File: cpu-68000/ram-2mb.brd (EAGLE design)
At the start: 160 x 100 mm, 54 parts, among them IC101 74HC245DW, IC102 74HC245DW, IC103 74HC245DW, IC104 74HC245DW

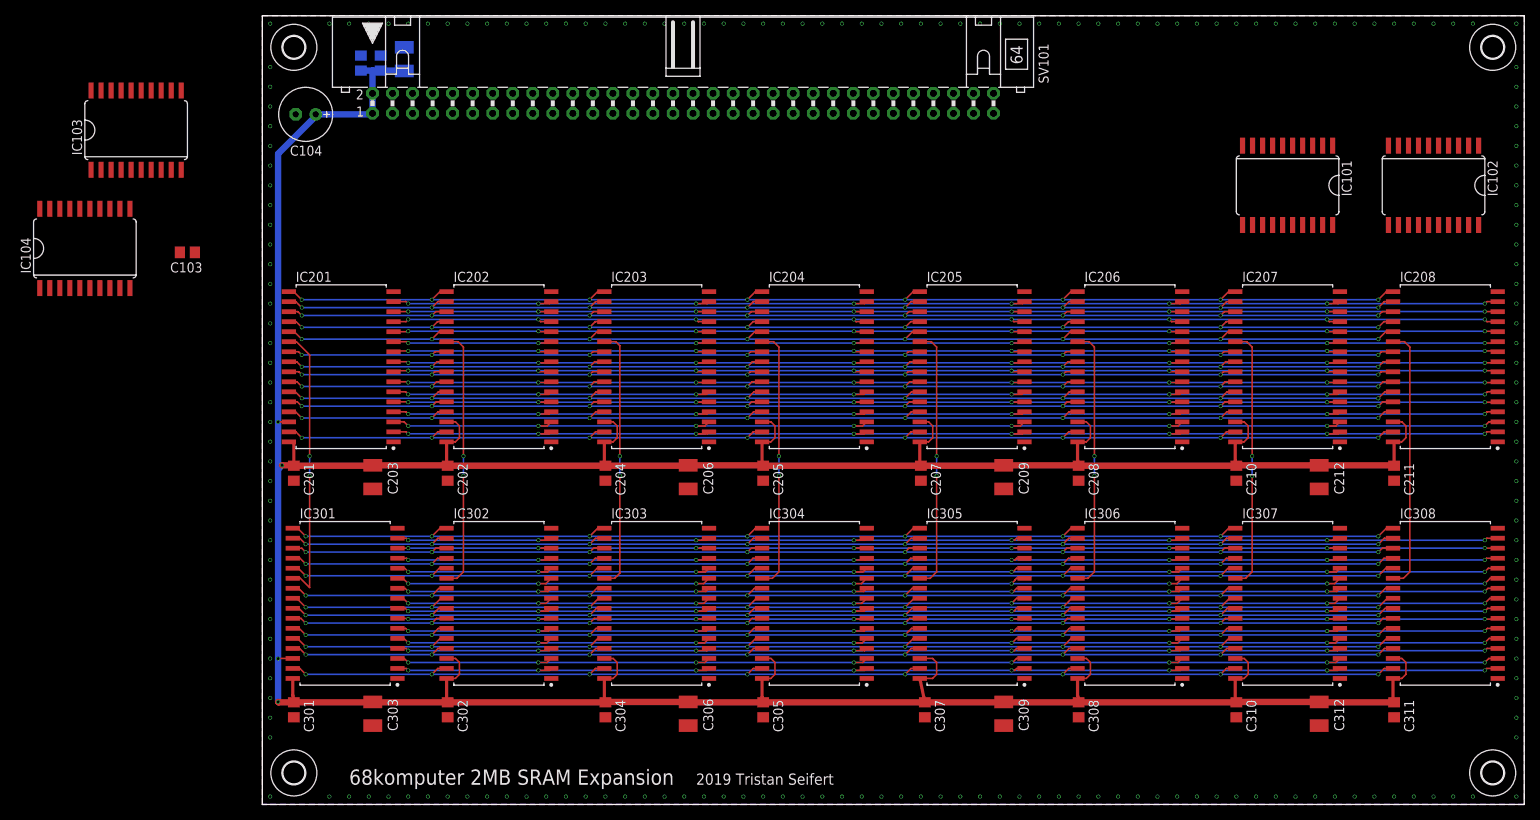
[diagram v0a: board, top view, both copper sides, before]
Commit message: 2MB RAM Expansion: 	- Added decoding logic 	- Started routing bus transceivers 	- Fixed SRAM footprint
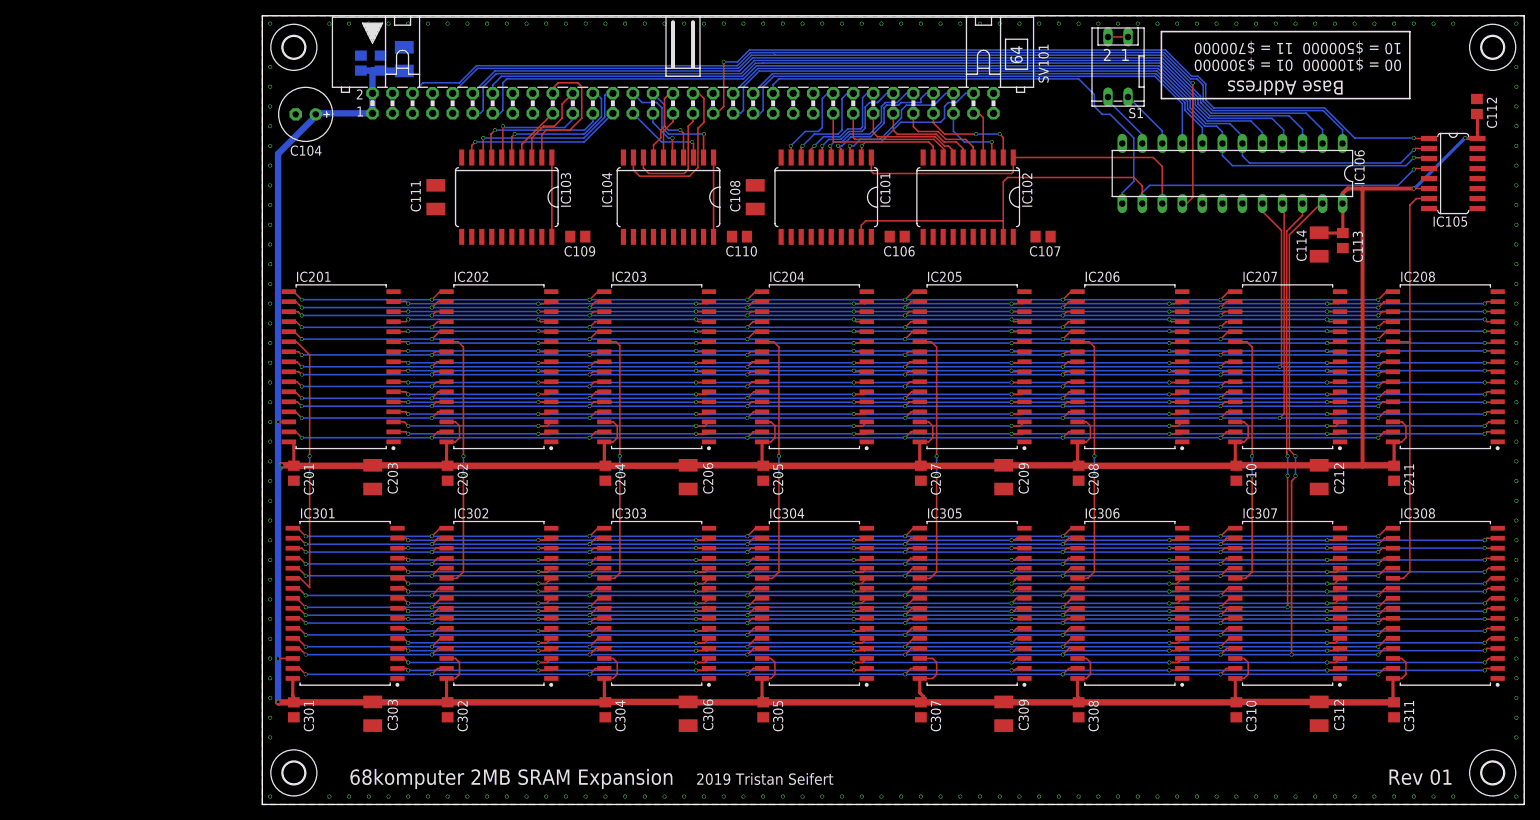
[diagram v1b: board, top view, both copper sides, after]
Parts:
- removed C103: 100nF, rcl:C0805
- added C106, C107, C109, C110, C112, C113: 100nF, rcl:C0805
- added C108, C111, C114: 10µF, rcl:SMC_B
- added IC105: 74HC138D, 74xx-eu:SO16
- added IC106: GAL22V10D, 68komputer:DIL24S
- added S1: (no value), switch-dil:DP-02
- moved IC104 74.3 mm to (51.5, 77.0), turned to 180 degrees
- moved IC102 59.0 mm to (89.5, 77.0)
- moved IC101 58.5 mm to (71.5, 77.0)
- moved IC103 47.8 mm to (31.0, 77.0), turned to 180 degrees
- moved C307 0.50 mm to (83.5, 12.0)
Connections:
- removed net VCC: IC101.20, IC102.20, IC103.20, IC104.20
- new net !CS: IC101.19, IC102.19, IC103.19, IC104.19, IC105.4, IC106.14
- new net !RD: IC101.1, IC102.1, IC106.15
- new net ADDR_SET0: IC106.10, S1.4
- new net ADDR_SET1: IC106.11, S1.3
- new net N$5: IC106.19
- new net N$6: IC106.18
- new net N$7: IC106.17
- net !AS: now also IC106.5
- net !DTACK: now also IC106.16
- net !LDS: now also IC106.3
- net !LOE: now also IC106.20
- net !LWE: now also IC106.21
- net !RAM_CS0: now also IC105.15
- net !RAM_CS1: now also IC105.14
- net !RAM_CS2: now also IC105.13
- net !RAM_CS3: now also IC105.12
- net !RAM_CS4: now also IC105.11
- net !RAM_CS5: now also IC105.10
- net !RAM_CS6: now also IC105.9
- net !RAM_CS7: now also IC105.7
- net !RESET: now also IC106.1
- net !UDS: now also IC106.4
- net !UOE: now also IC106.22
- net !UWE: now also IC106.23
- net +5V: now also C106.1, C107.1, C108.+, C109.1, C110.1, C111.+, C112.1, C113.1, C114.+, IC101.20, IC102.20, IC103.1, IC103.20, IC104.1, IC104.20, IC105.16, IC105.6, IC106.24, S1.1, S1.2; no longer C103.1
- net A1: now also IC103.2
- net A10: now also IC104.3
- net A11: now also IC104.4
- net A12: now also IC104.5
- net A13: now also IC104.6
- net A14: now also IC104.7
- net A15: now also IC104.8
- net A16: now also IC104.9
- net A18: now also IC105.1
- net A19: now also IC105.2, IC106.6
- net A2: now also IC103.3
- net A20: now also IC105.3, IC106.7
- net A21: now also IC106.8
- net A22: now also IC106.9
- net A23: now also IC106.13
- net A3: now also IC103.4
- net A4: now also IC103.5
- net A5: now also IC103.6
- net A6: now also IC103.7
- net A7: now also IC103.8
- net A8: now also IC103.9
- net A9: now also IC104.2
- net D0: now also IC101.2
- net D1: now also IC101.3
- net D10: now also IC102.4
- net D11: now also IC102.5
- net D12: now also IC102.6
- net D13: now also IC102.7
- net D14: now also IC102.8
- net D15: now also IC102.9
- net D2: now also IC101.4
- net D3: now also IC101.5
- net D4: now also IC101.6
- net D5: now also IC101.7
- net D6: now also IC101.8
- net D7: now also IC101.9
- net D8: now also IC102.2
- net D9: now also IC102.3
- net GND: now also C106.2, C107.2, C108.-, C109.2, C110.2, C111.-, C112.2, C113.2, C114.-, IC105.5, IC105.8, IC106.12; no longer C103.2
- net R/!W!: now also IC106.2
- net RAM_A0: now also IC103.18
- net RAM_A1: now also IC103.17
- net RAM_A10: now also IC104.16
- net RAM_A11: now also IC104.15
- net RAM_A12: now also IC104.14
- net RAM_A13: now also IC104.13
- net RAM_A14: now also IC104.12
- net RAM_A15: now also IC104.11
- net RAM_A2: now also IC103.16
- net RAM_A3: now also IC103.15
- net RAM_A4: now also IC103.14
- net RAM_A5: now also IC103.13
- net RAM_A6: now also IC103.12
- net RAM_A7: now also IC103.11
- net RAM_A8: now also IC104.18
- net RAM_A9: now also IC104.17
- net RAM_D0: now also IC101.18
- net RAM_D1: now also IC101.17
- net RAM_D10: now also IC102.16
- net RAM_D11: now also IC102.15
- net RAM_D12: now also IC102.14
- net RAM_D13: now also IC102.13
- net RAM_D14: now also IC102.12
- net RAM_D15: now also IC102.11
- net RAM_D2: now also IC101.16
- net RAM_D3: now also IC101.15
- net RAM_D4: now also IC101.14
- net RAM_D5: now also IC101.13
- net RAM_D6: now also IC101.12
- net RAM_D7: now also IC101.11
- net RAM_D8: now also IC102.18
- net RAM_D9: now also IC102.17
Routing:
- net !RESET: track 0.00 -> 127.0 mm
- net !LDS: track 0.00 -> 115.7 mm
- net R/!W!: track 0.00 -> 115.6 mm
- net !DTACK: track 0.00 -> 113.5 mm, vias 0 -> 1
- net !UDS: track 0.00 -> 108.3 mm
- net !AS: track 0.00 -> 107.6 mm
- net A18: track 0.00 -> 103.2 mm, vias 0 -> 2
- net A20: track 0.00 -> 99.9 mm, vias 0 -> 1
- net A19: track 0.00 -> 97.3 mm, vias 0 -> 1
- net +5V: track 505.1 -> 597.3 mm, vias 4 -> 6
- net !CS: track 0.00 -> 86.2 mm, vias 0 -> 1
- net A22: track 0.00 -> 64.7 mm
- net A21: track 0.00 -> 63.4 mm
- net A23: track 0.00 -> 60.0 mm
- net !UWE: track 153.3 -> 212.9 mm, vias 8 -> 11
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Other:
- board text added: "00 = $100000 01 = $300000 10 = $500000 11 = $700000"
- board text added: "Base Address"
- board text added: "Rev 01"

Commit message: 2MB RAM Expansion: 	- Finished routing all signals
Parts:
- added C115, C116: 100nF, rcl:C0805
- added IC107: 74HC243D, 74xx-eu:SO14
- added LED101: (no value), led:CHIPLED_1206
- added R101, R102: 10k, rcl:R2012
- added R103: 3k, rcl:R2012
- moved C206 1.00 mm to (55.0, 41.5)
- moved C306 1.00 mm to (55.0, 11.5)
- moved C209 0.50 mm to (94.5, 41.5)
- moved C309 0.50 mm to (94.5, 11.5)
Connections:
- new net N$18: LED101.A, R103.2
- net !CS: now also IC107.1
- net +5V: now also C115.1, C116.1, IC107.13, IC107.14, R103.1
- net A17: now also IC107.3
- net ADDR_SET0: now also R102.1
- net ADDR_SET1: now also R101.1
- net GND: now also C115.2, C116.2, IC107.4, IC107.5, IC107.6, IC107.7, LED101.C, R101.2, R102.2
- net RAM_A16: now also IC107.11
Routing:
- net !RAM_CS0: track 35.5 -> 269.8 mm
- net !RAM_CS1: track 33.4 -> 249.8 mm
- net +5V: track 597.3 -> 803.5 mm, vias 6 -> 37
- net !RAM_CS2: track 33.3 -> 229.2 mm
- net !RAM_CS3: track 33.4 -> 209.7 mm
- net !RAM_CS4: track 33.4 -> 189.7 mm
- net !RAM_CS5: track 33.4 -> 169.4 mm
- net !RAM_CS6: track 33.4 -> 149.2 mm
- net RAM_A16: track 300.8 -> 375.7 mm, vias 16 -> 18
- net !CS: track 86.2 -> 158.0 mm, vias 1 -> 6
- net A17: track 0.00 -> 60.4 mm
- net RAM_A15: track 306.8 -> 362.6 mm, vias 16 -> 18
- net RAM_A14: track 302.5 -> 356.7 mm, vias 16 -> 18
- net RAM_A12: track 301.0 -> 354.4 mm, vias 16 -> 18
- net RAM_A8: track 307.3 -> 359.9 mm, vias 16 -> 18
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
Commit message: CPU board: 	- Clean up some traces
IO board:
	- Started work on super IO board
	- UARTs, parallel port, PS/2 keyboard/mouse interface, I2C

2MB RAM Expansion:
	- Added some address decoding
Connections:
- new net !EXT_ID: SV101.41
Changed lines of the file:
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@@
 <wire x1="3.5" y1="76.25" x2="3.5" y2="73.85" width="0.2032" layer="1"/>
+</signal>
+<signal name="!EXT_ID">
+<contactref element="SV101" pad="41"/>
 </signal>
 </signals>

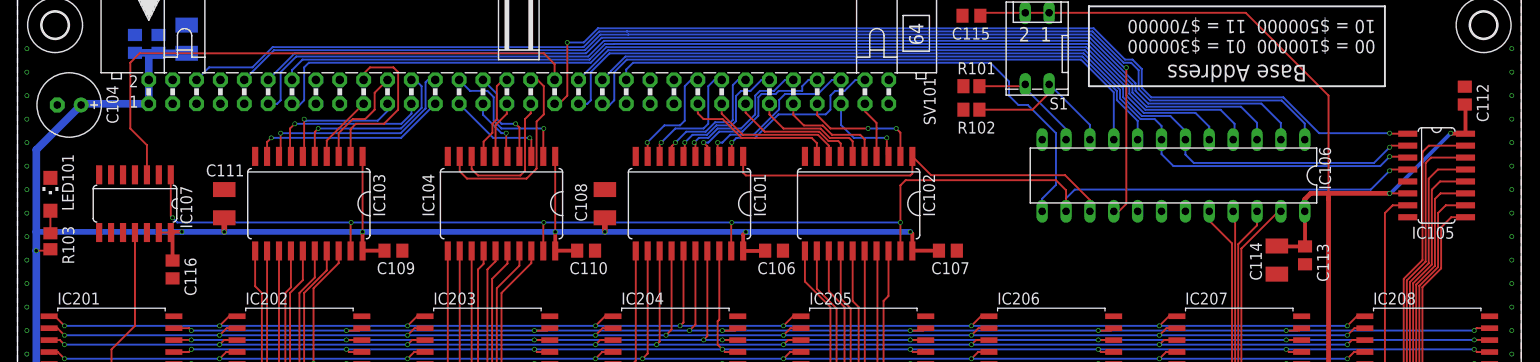
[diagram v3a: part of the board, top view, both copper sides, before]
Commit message: IO board: 	- Added 82C55 PIO
RAM board:
	- Tweaked tolerances between some traces
	- Fixed naming of parts
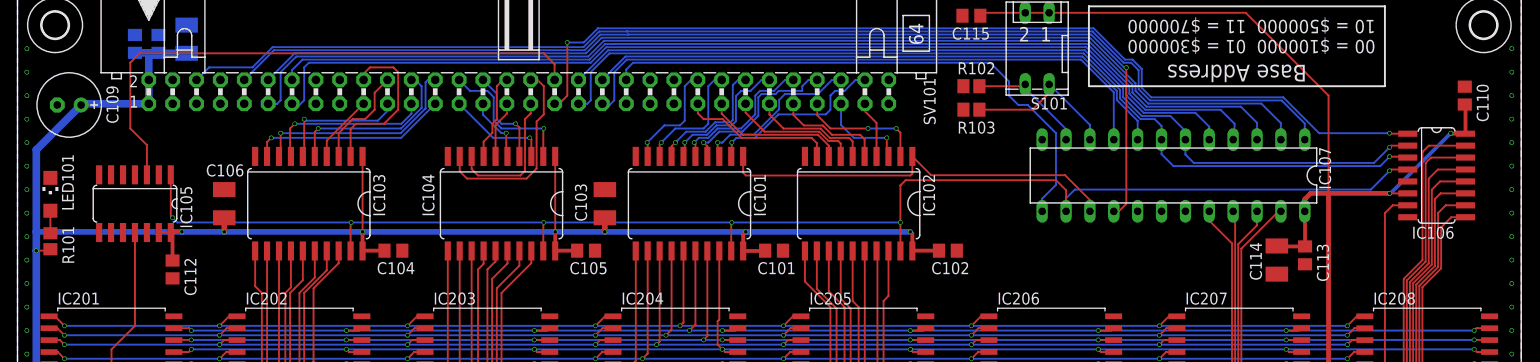
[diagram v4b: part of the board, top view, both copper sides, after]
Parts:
- removed C116: 100nF, rcl:C0805
- added C103: 10µF, rcl:SMC_B
- C102: value 1µF -> 100nF
- C104: value 120µF -> 100nF; device rcl:E2,5-7 -> rcl:C0805
- C105: value 10µF -> 100nF; device rcl:SMC_B -> rcl:C0805
- C106: value 100nF -> 10µF; device rcl:C0805 -> rcl:SMC_B
- C108: value 10µF -> 1µF; device rcl:SMC_B -> rcl:C0805
- C109: value 100nF -> 120µF; device rcl:C0805 -> rcl:E2,5-7
- IC105: value 74HC138D -> 74HC243D; device 74xx-eu:SO16 -> 74xx-eu:SO14
- IC106: value GAL22V10D -> 74HC138D; device 68komputer:DIL24S -> 74xx-eu:SO16
- IC107: value 74HC243D -> GAL22V10D; device 74xx-eu:SO14 -> 68komputer:DIL24S
- R101: value 10k -> 3k
- R103: value 3k -> 10k
- moved C112 138.7 mm to (16.5, 70.0), turned to 270 degrees
- moved IC105 138.5 mm to (12.5, 77.0), turned to 180 degrees
- moved IC107 110.5 mm to (123.0, 80.0)
- moved R101 99.4 mm to (3.50, 73.0), turned to 90 degrees
- moved R103 99.0 mm to (101.5, 87.0), turned to 180 degrees
- moved C110 94.9 mm to (154.0, 88.5), turned to 90 degrees
- moved C102 89.3 mm to (99.0, 72.0), flipped to the top, turned to 0 degrees
- moved C107 86.8 mm to (15.0, 94.0), flipped to the bottom, turned to 90 degrees
- moved C101 69.1 mm to (80.5, 72.0), flipped to the top, turned to 0 degrees
- moved C106 58.7 mm to (22.0, 77.0), turned to 90 degrees
- moved C108 52.8 mm to (12.5, 94.0), flipped to the bottom
- moved C105 48.1 mm to (60.5, 72.0), flipped to the top, turned to 0 degrees
- moved C104 37.8 mm to (40.0, 72.0), turned to 0 degrees
- moved C109 37.8 mm to (5.50, 87.5), turned to 180 degrees
- moved IC106 28.0 mm to (151.0, 80.0), turned to 270 degrees
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- renumbered S1 to S101
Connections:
- net !AS: now also IC107.5; no longer IC106.5
- net !CS: now also IC105.1, IC106.4, IC107.14; no longer IC105.4, IC106.14, IC107.1
- net !DTACK: now also IC107.16; no longer IC106.16
- net !LDS: now also IC107.3; no longer IC106.3
- net !LOE: now also IC107.20; no longer IC106.20
- net !LWE: now also IC107.21; no longer IC106.21
- net !RAM_CS0: now also IC106.15; no longer IC105.15
- net !RAM_CS1: now also IC106.14; no longer IC105.14
- net !RAM_CS2: now also IC106.13; no longer IC105.13
- net !RAM_CS3: now also IC106.12; no longer IC105.12
- net !RAM_CS4: now also IC106.11; no longer IC105.11
- net !RAM_CS5: now also IC106.10; no longer IC105.10
- net !RAM_CS6: now also IC106.9; no longer IC105.9
- net !RAM_CS7: now also IC106.7; no longer IC105.7
- net !RD: now also IC107.15; no longer IC106.15
- net !RESET: now also IC107.1; no longer IC106.1
- net !UDS: now also IC107.4; no longer IC106.4
- net !UOE: now also IC107.22; no longer IC106.22
- net !UWE: now also IC107.23; no longer IC106.23
- net +5V: now also C103.+, C104.1, C105.1, C106.+, C108.1, C109.+, IC105.13, IC105.14, IC106.16, IC106.6, IC107.24, R101.1; no longer C104.+, C105.+, C106.1, C108.+, C109.1, C116.1, IC105.16, IC105.6, IC106.24, IC107.13, IC107.14, R103.1
- net A17: now also IC105.3; no longer IC107.3
- net A18: now also IC106.1; no longer IC105.1
- net A19: now also IC106.2, IC107.6; no longer IC105.2, IC106.6
- net A20: now also IC106.3, IC107.7; no longer IC105.3, IC106.7
- net A21: now also IC107.8; no longer IC106.8
- net A22: now also IC107.9; no longer IC106.9
- net A23: now also IC107.13; no longer IC106.13
- net ADDR_SET0: now also IC107.10, R103.1; no longer IC106.10, R102.1
- net ADDR_SET1: now also IC107.11, R102.1; no longer IC106.11, R101.1
- net GND: now also C103.-, C104.2, C105.2, C106.-, C108.2, C109.-, IC105.4, IC105.6, IC105.7, IC106.5, IC106.8, IC107.12, R103.2; no longer C104.-, C105.-, C106.2, C108.-, C109.2, C116.2, IC105.8, IC106.12, IC107.4, IC107.5, IC107.6, IC107.7, R101.2
- net N$18: now also R101.2; no longer R103.2
- net N$5: now also IC107.19; no longer IC106.19
- net N$6: now also IC107.18; no longer IC106.18
- net N$7: now also IC107.17; no longer IC106.17
- net R/!W!: now also IC107.2; no longer IC106.2
- net RAM_A16: now also IC105.11; no longer IC107.11
